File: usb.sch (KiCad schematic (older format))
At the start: 3 parts, among them J4 USB_OTG, J5 Conn_01x06, Y1 Crystal_GND24

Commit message: flash chip
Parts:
- Y1: value Crystal_GND24 -> FNETHE025
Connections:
- net +3V3: now also J5.1 (Pin_1)
- net GND: now also J5.2 (Pin_2)
- net JTAG_TCK: now reaches J5.3 (Pin_3)
- net JTAG_TDO: now reaches J5.4 (Pin_4)
- net JTAG_TDI: now reaches J5.5 (Pin_5)
- net JTAG_TMS: now reaches J5.6 (Pin_6)
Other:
- moved on the sheet: J5
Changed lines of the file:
@@
 $Descr A4 11693 8268
 encoding utf-8
-Sheet 4 5
+Sheet 4 6
 Title ""
 Date ""
@@
 F 1 "USB_OTG" H 2250 2900 50  0000 L CNN
 F 2 "usb_otg:USB-MICRO-B-FCI-10118192-0001LF" H 2600 2500 50  0001 C CNN
-F 3 "" H 2600 2500 50  0001 C CNN
+F 3 "portal.fciconnect.com/Comergent/fci/drawing/10118192.pdf" H 2600 2500 50  0001 C CNN
 	1    2450 2550
 	1    0    0    -1
@@
 P 3550 4050
 F 0 "Y1" H 3675 4250 50  0000 L CNN
-F 1 "Crystal_GND24" H 3675 4175 50  0000 L CNN
+F 1 "FNETHE025" H 3675 4175 50  0000 L CNN
 F 2 "oscxo:Crystal_SMD_7050_4Pads" H 3550 4050 50  0001 C CNN
 F 3 "" H 3550 4050 50  0001 C CNN
@@
 F 3 "" H 3700 1450 50  0001 C CNN
 	1    3700 1450
-	1    0    0    -1
+	-1   0    0    -1
 $EndComp
+$Comp
+L +3V3 #PWR06
+U 1 1 5A12F29D
+P 3900 1250
+F 0 "#PWR06" H 3900 1100 50  0001 C CNN
+F 1 "+3V3" H 3900 1390 50  0000 C CNN
+F 2 "" H 3900 1250 50  0001 C CNN
+F 3 "" H 3900 1250 50  0001 C CNN
+	1    3900 1250
+	0    1    1    0
+$EndComp
+$Comp
+L GND #PWR07
+U 1 1 5A12F2BA
+P 3900 1350
+F 0 "#PWR07" H 3900 1100 50  0001 C CNN
+F 1 "GND" H 3900 1200 50  0000 C CNN
+F 2 "" H 3900 1350 50  0001 C CNN
+F 3 "" H 3900 1350 50  0001 C CNN
+	1    3900 1350
+	0    -1   -1   0
+$EndComp
+Text GLabel 3900 1450 2    60   Input ~ 0
+JTAG_TCK
+Text GLabel 3900 1550 2    60   Input ~ 0
+JTAG_TDO
+Text GLabel 3900 1750 2    60   Input ~ 0
+JTAG_TMS
+Text GLabel 3900 1650 2    60   Input ~ 0
+JTAG_TDI
 $EndSCHEMATC

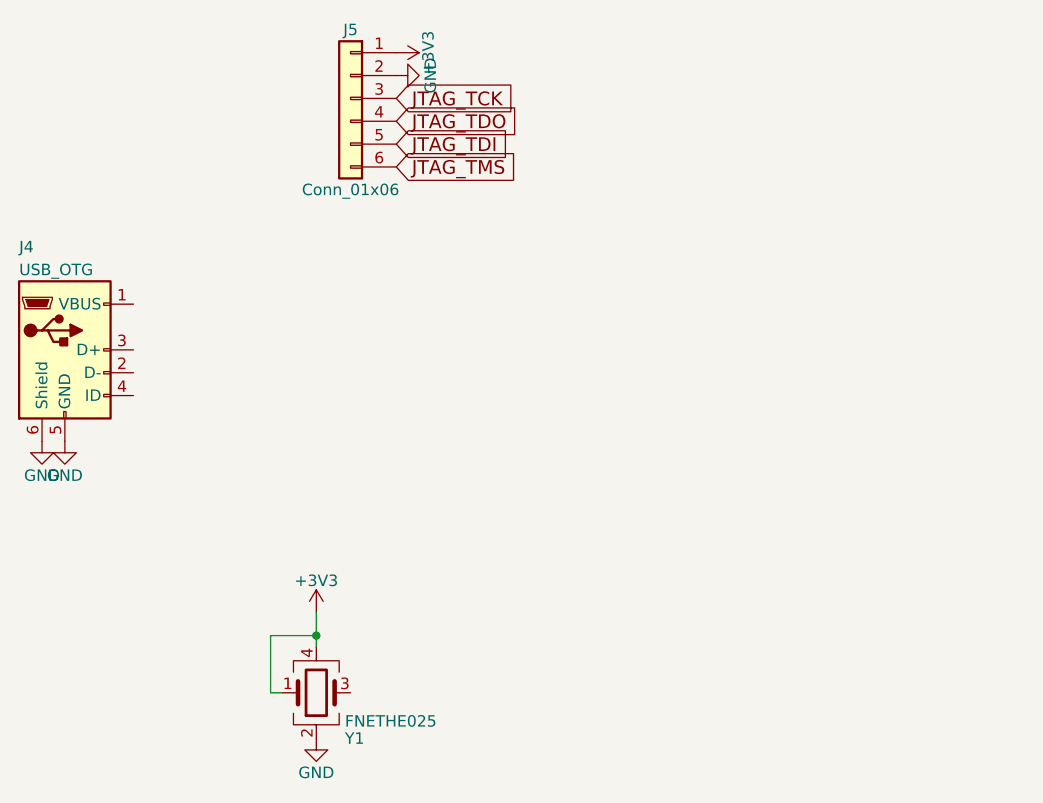
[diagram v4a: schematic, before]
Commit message: usbserial chip ft232rl
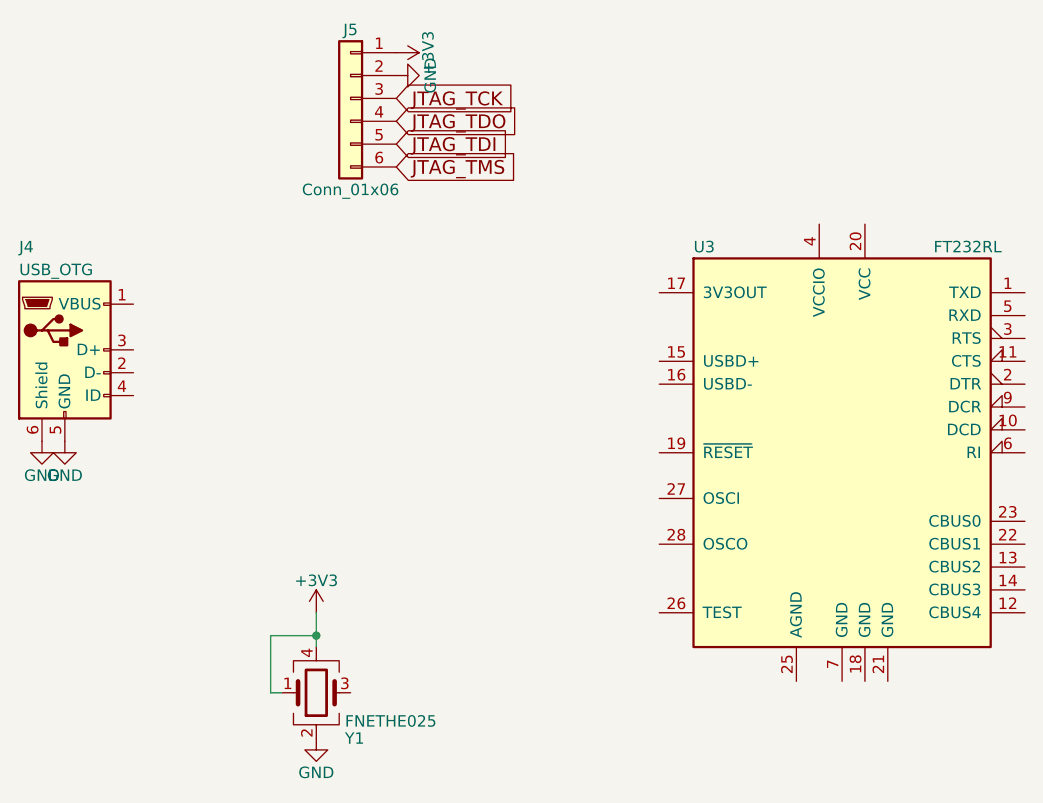
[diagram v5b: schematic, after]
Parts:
- added U3: FT232RL, Housings_SSOP:SSOP-28_5.3x10.2mm_Pitch0.65mm, symbol FT232RL
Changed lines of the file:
@@
 LIBS:valves
 LIBS:lfxp2-xe-xtn144x
+LIBS:ftdi
 LIBS:ulx2s-cache
 EELAYER 25 0
@@
 Text GLabel 3900 1650 2    60   Input ~ 0
 JTAG_TDI
+$Comp
+L FT232RL U3
+U 1 1 5A1333CB
+P 5850 3000
+F 0 "U3" H 5200 3900 50  0000 L CNN
+F 1 "FT232RL" H 6250 3900 50  0000 L CNN
+F 2 "Housings_SSOP:SSOP-28_5.3x10.2mm_Pitch0.65mm" H 5850 3000 50  0001 C CNN
+F 3 "" H 5850 3000 50  0001 C CNN
+	1    5850 3000
+	1    0    0    -1
+$EndComp
 $EndSCHEMATC
